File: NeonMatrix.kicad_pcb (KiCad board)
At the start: 2 copper layers, 116 x 116 mm, 282 parts, among them J1 Mains, J2 Data, M1 B0505S, U1 74HC595, U10 ADuM1200AR, U2 74HC595, U3 74HC595, U4 74HC595, U5 74HC595, U6 74HC595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

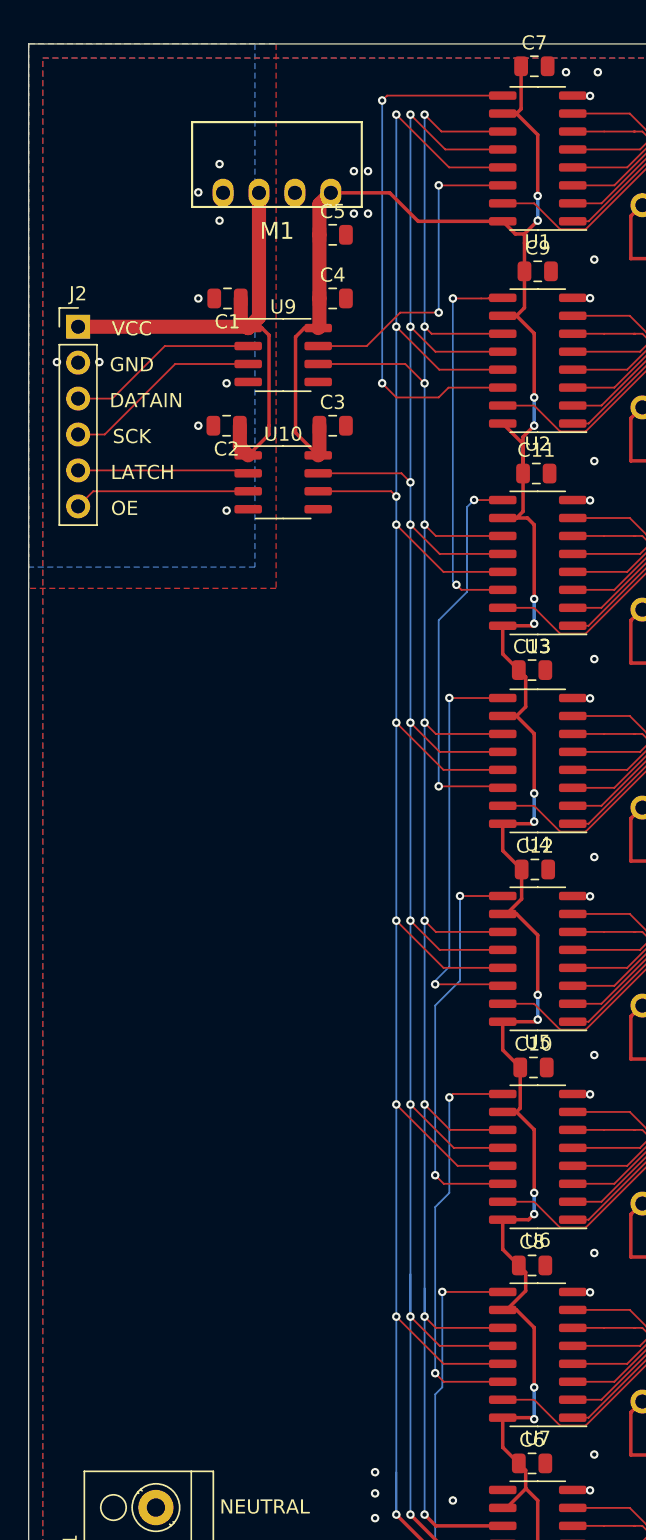
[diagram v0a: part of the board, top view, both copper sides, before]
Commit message: Add PCB markings
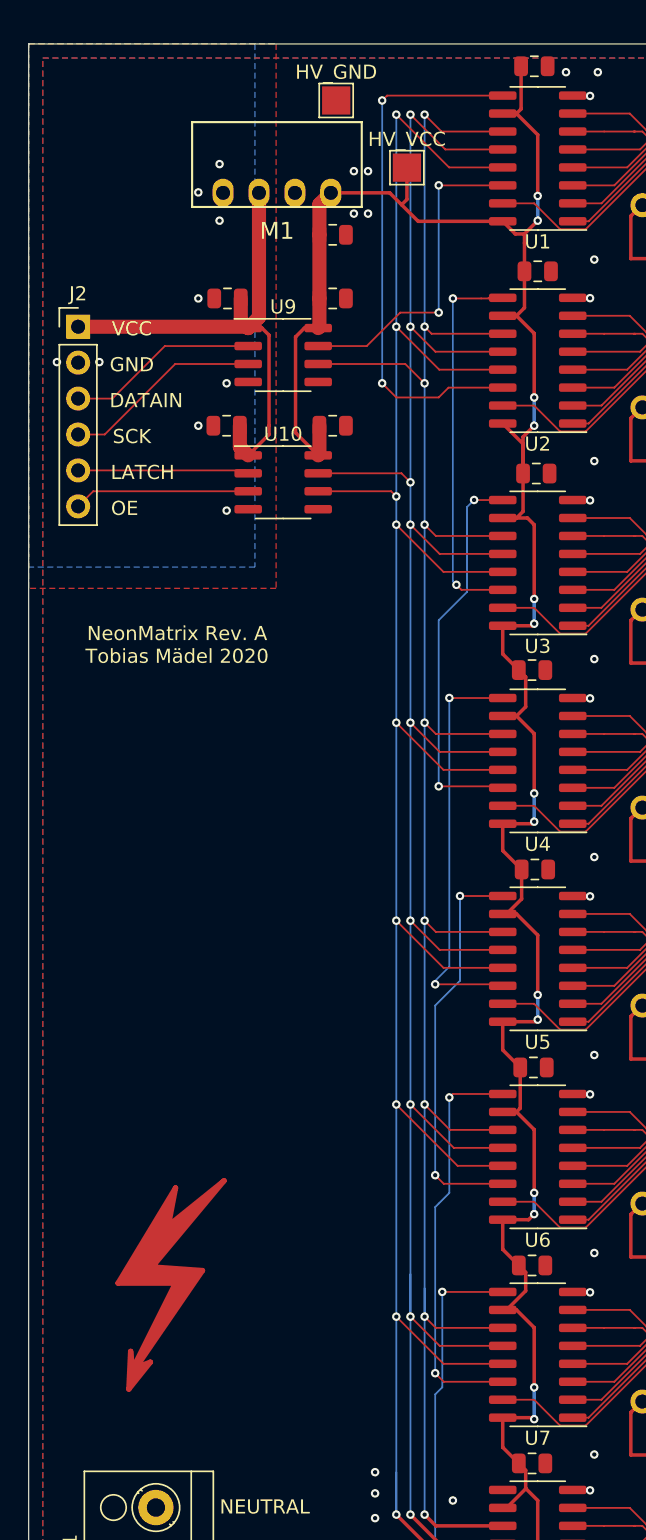
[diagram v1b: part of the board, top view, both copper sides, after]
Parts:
- added FID2: HV, Symbol:Symbol_HighVoltage_Type1_CopperTop_Big, F.Cu at (157.5, 118.2)
- added HV_GND: HV_GND, TestPoint:TestPoint_Pad_2.0x2.0mm, F.Cu at (169.8, 35.0)
- added HV_VCC: HV_VCC, TestPoint:TestPoint_Pad_2.0x2.0mm, F.Cu at (174.8, 39.7)
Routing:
- net +3V3: track 186.5 -> 189.3 mm
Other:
- board text added: "NeonMatrix Rev. A Tobias Mädel 2020"
- board text added: "tbspace.de"

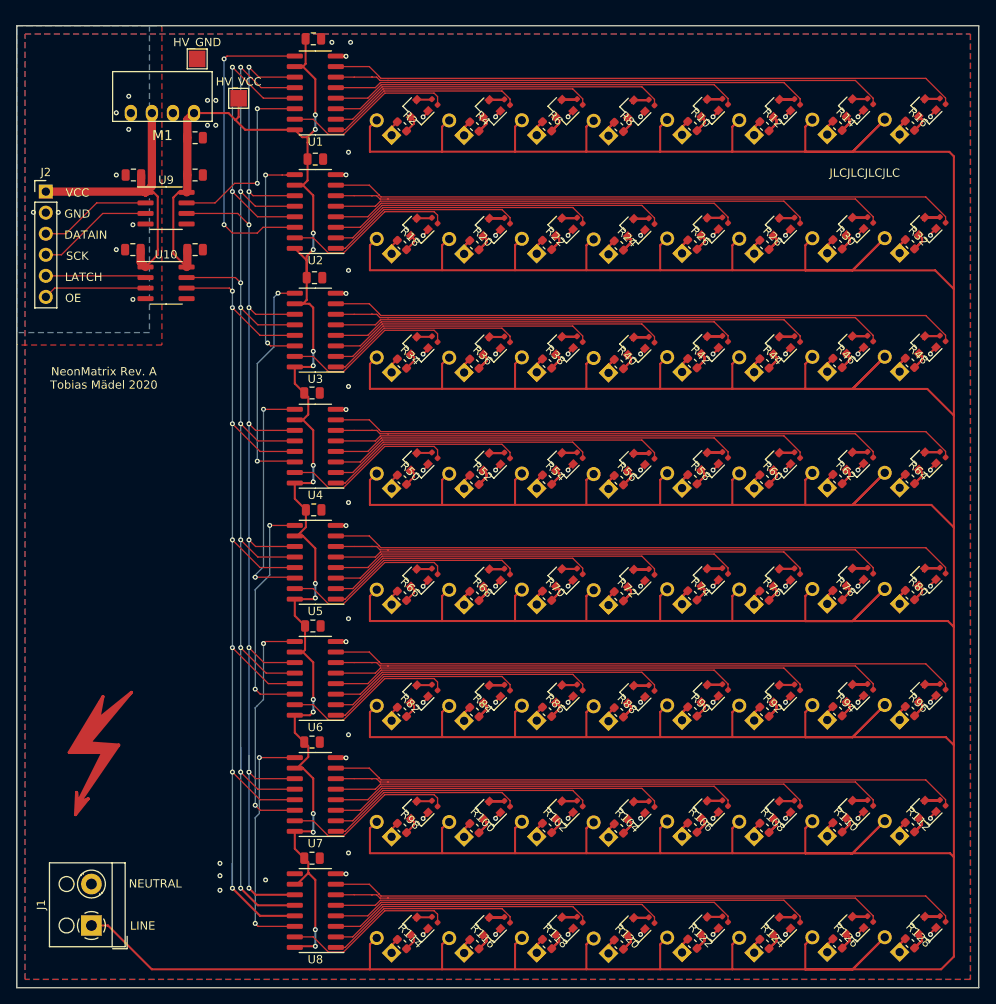
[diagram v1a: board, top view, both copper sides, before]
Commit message: Add bulk capacitance, fix isolation, silkscreen and vias
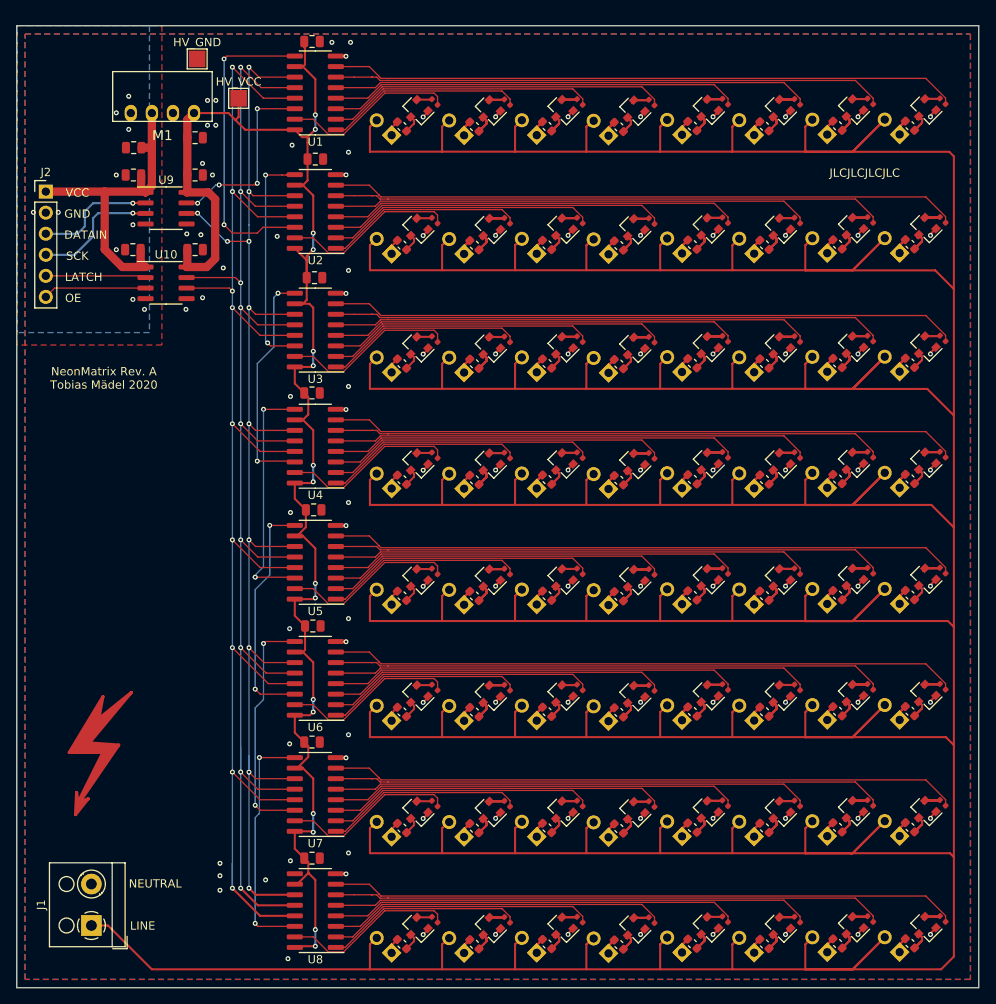
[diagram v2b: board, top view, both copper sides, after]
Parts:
- added C14: 22u, Capacitor_SMD:C_0805_2012Metric, F.Cu at (162.1, 45.7)
- moved C7 0.36 mm to (183.6, 32.9)
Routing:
- net +3V3: track 189.3 -> 192.9 mm
- net /ISO_5V: track 37.4 -> 40.6 mm
- net /ISO_SCK: track 14.1 -> 15.4 mm, vias 0 -> 1
- net /ISO_DATAIN: track 13.6 -> 14.6 mm, vias 0 -> 1
- net /SCK: track 156.4 -> 157.2 mm, vias 9 -> 11
- net /DATAIN: track 23.0 -> 23.1 mm, vias 2 -> 4
- net GND: vias 89 -> 104
- net /ISO_GND: vias 9 -> 10

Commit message: RevA, Add production files
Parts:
- added C15: 100n, Capacitor_SMD:C_0805_2012Metric, F.Cu at (162.3, 73.8)
- added C16: 100n, Capacitor_SMD:C_0805_2012Metric, F.Cu at (169.5, 73.8)
- added U11: ADuM1200AR, Package_SO:SOIC-8_3.9x4.9mm_P1.27mm, F.Cu at (166.0, 70.1)
- J2: footprint Connector_PinHeader_2.54mm:PinHeader_1x06_P2.54mm_Vertical -> Connector_PinHeader_2.54mm:PinHeader_1x07_P2.54mm_Vertical
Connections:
- U8 pad 9: /sheet5EFAAFC6/DATAOUT -> /DATAOUT
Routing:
- net /DATAOUT: track 0.00 -> 74.2 mm, vias 0 -> 2
- net /ISO_5V: track 40.6 -> 60.4 mm
- net +3V3: track 192.9 -> 211.5 mm
- net /ISO_DATAOUT: track 0.00 -> 13.9 mm, vias 0 -> 1
- net /ISO_LATCH: track 12.1 -> 12.4 mm, vias 0 -> 1
- net /LATCH: track 168.3 -> 168.4 mm, vias 9 -> 11
- net /ISO_OE: vias 0 -> 1
- net GND: vias 104 -> 108
- net /ISO_GND: vias 10 -> 13
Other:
- board text added: "DATAOUT"
